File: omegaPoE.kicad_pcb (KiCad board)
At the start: 4 copper layers, 32.4 x 48 mm, 87 parts, among them J1 RJ45-TRANS_POE, J2 CONN_EXPANSION, J3 Conn_02x01, J4 Conn_02x01, Q1 FDM3622, Q2 Q_NMOS_GSD, SW1 SW_Push, T1 PA1276, U1 LM5070, U2 PS2501-1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

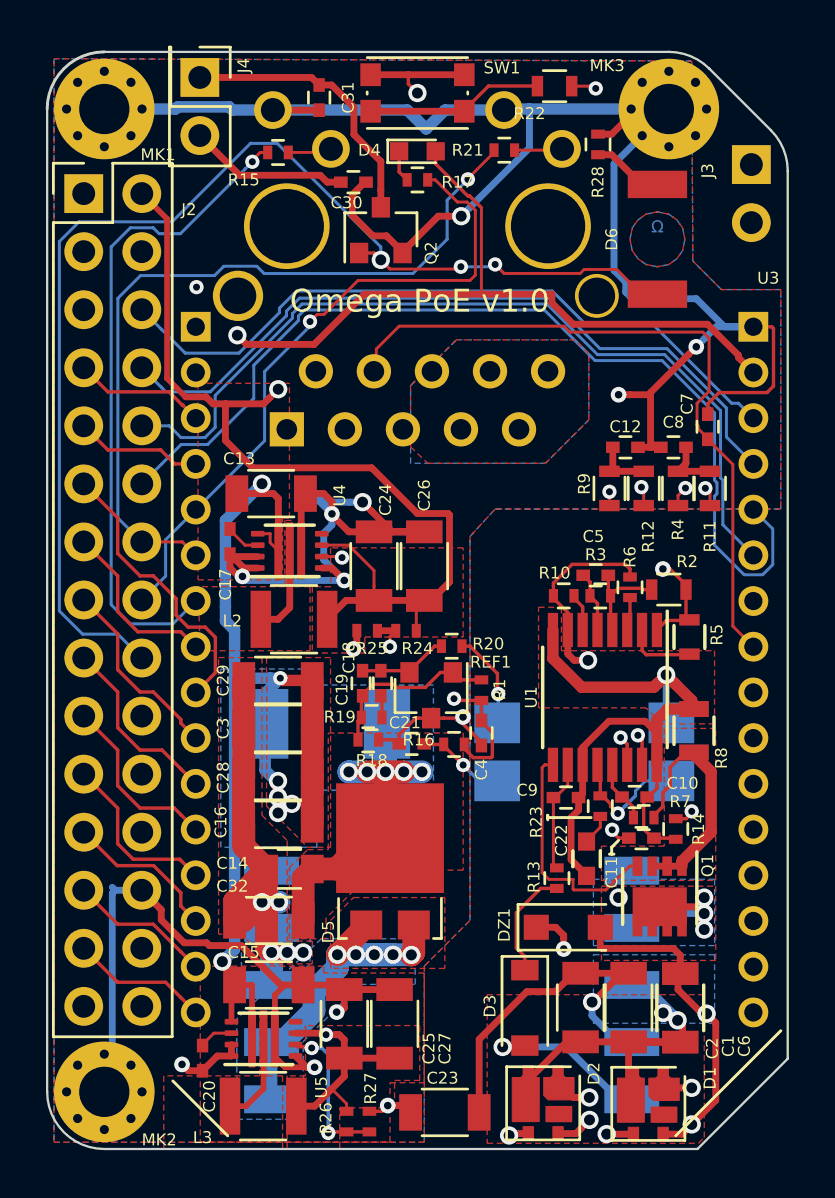
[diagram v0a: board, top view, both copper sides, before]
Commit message: Updated to kicad7
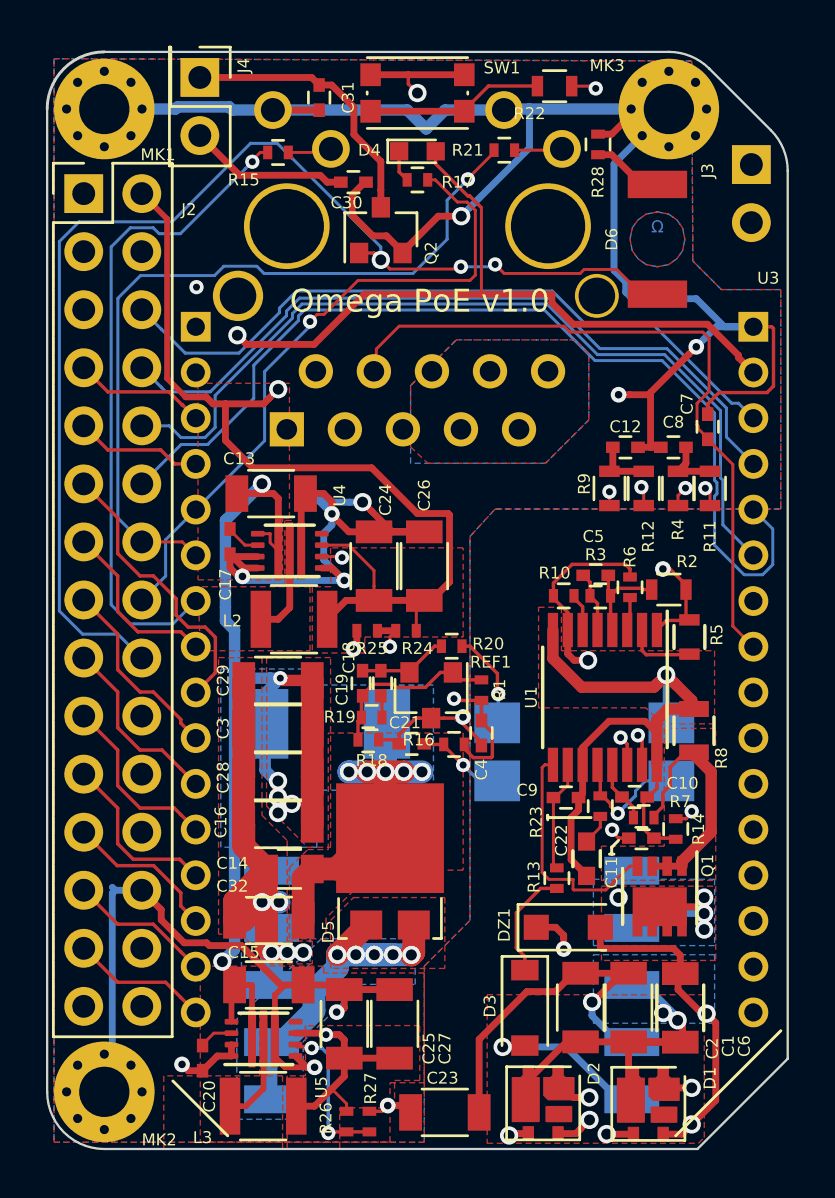
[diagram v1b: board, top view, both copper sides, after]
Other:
- net class Default removed
- net class ethernet_power removed
- net class power removed
